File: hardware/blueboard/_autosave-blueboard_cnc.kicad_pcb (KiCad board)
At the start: 2 copper layers, 199.4 x 198.9 mm, 108 parts, among them Q1 TRANSISTOR_NPN, Q2 TRANSISTOR_NPN, Q3 TRANSISTOR_NPN, SW1 SW_SPST

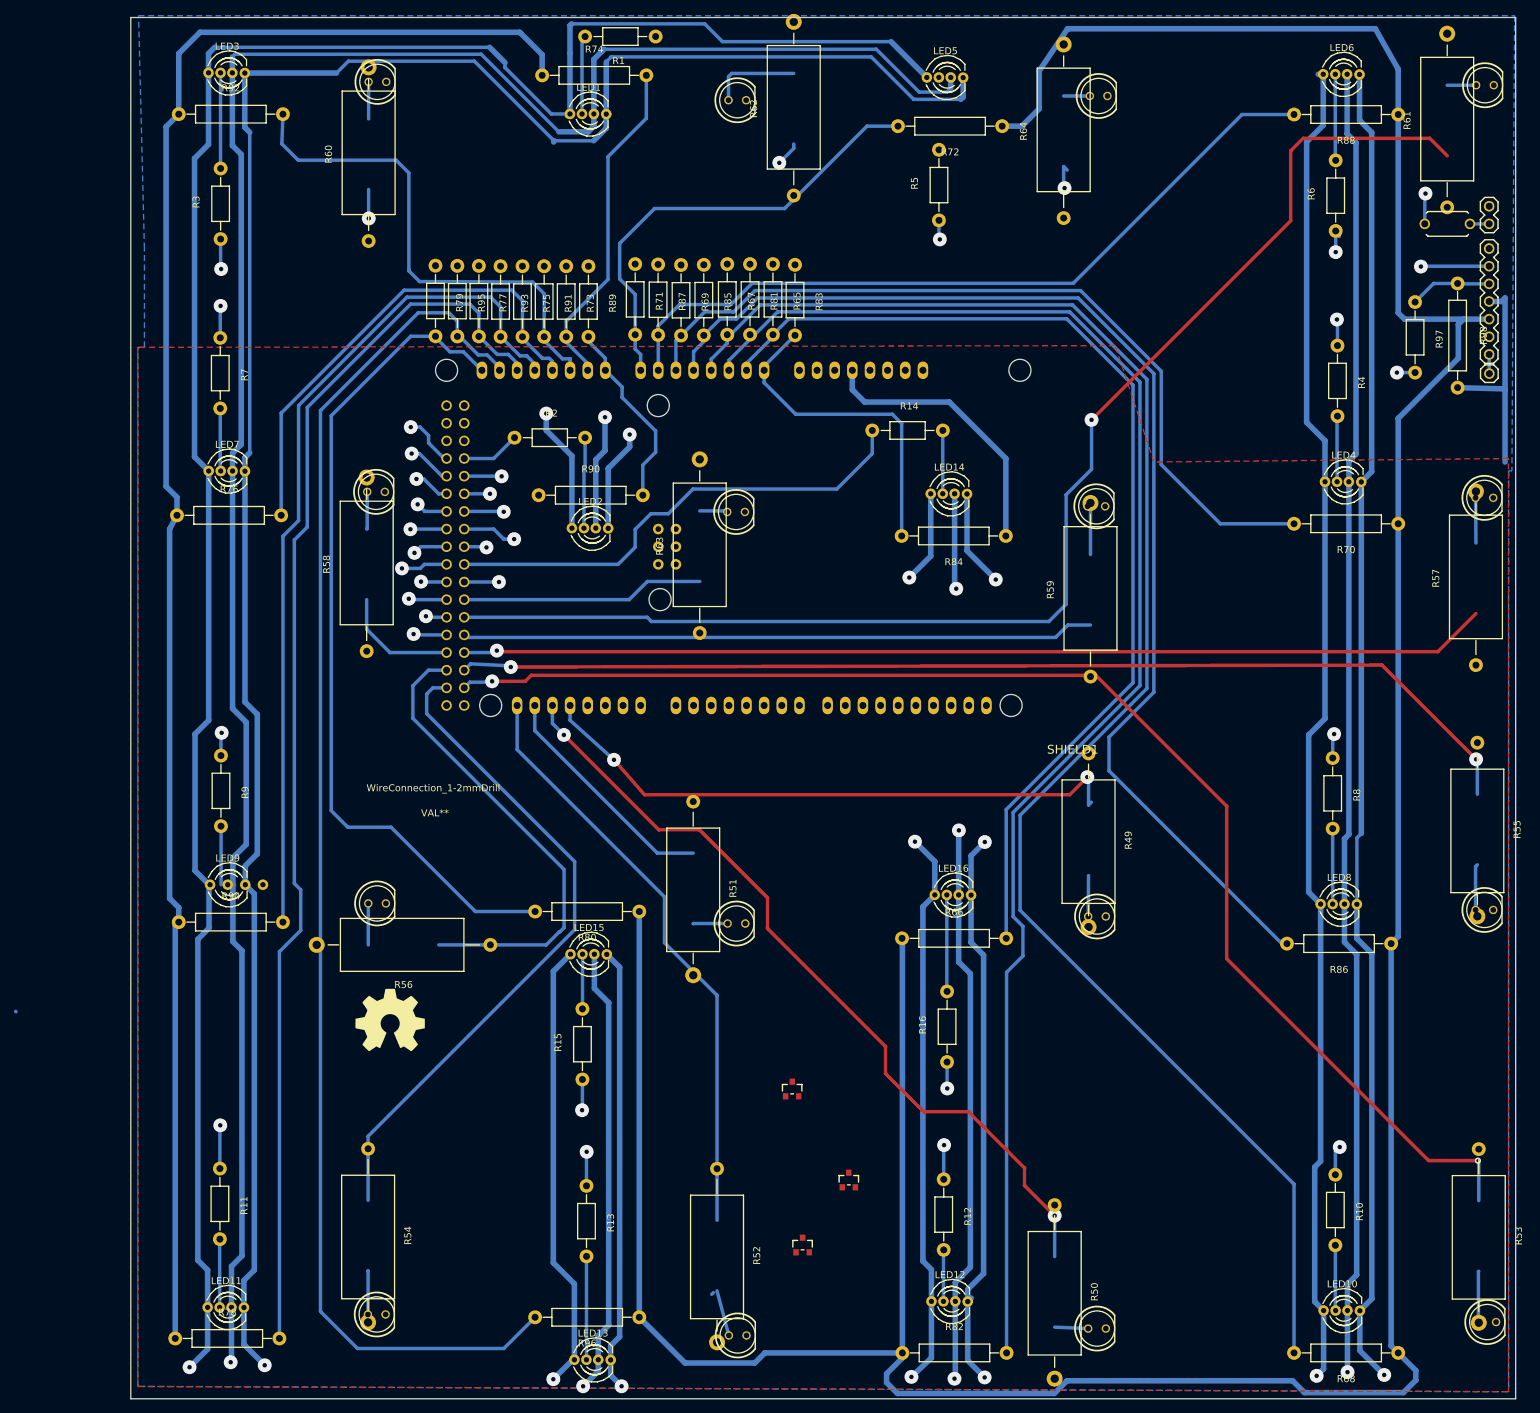
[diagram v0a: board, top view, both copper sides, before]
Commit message: state when board was cncd
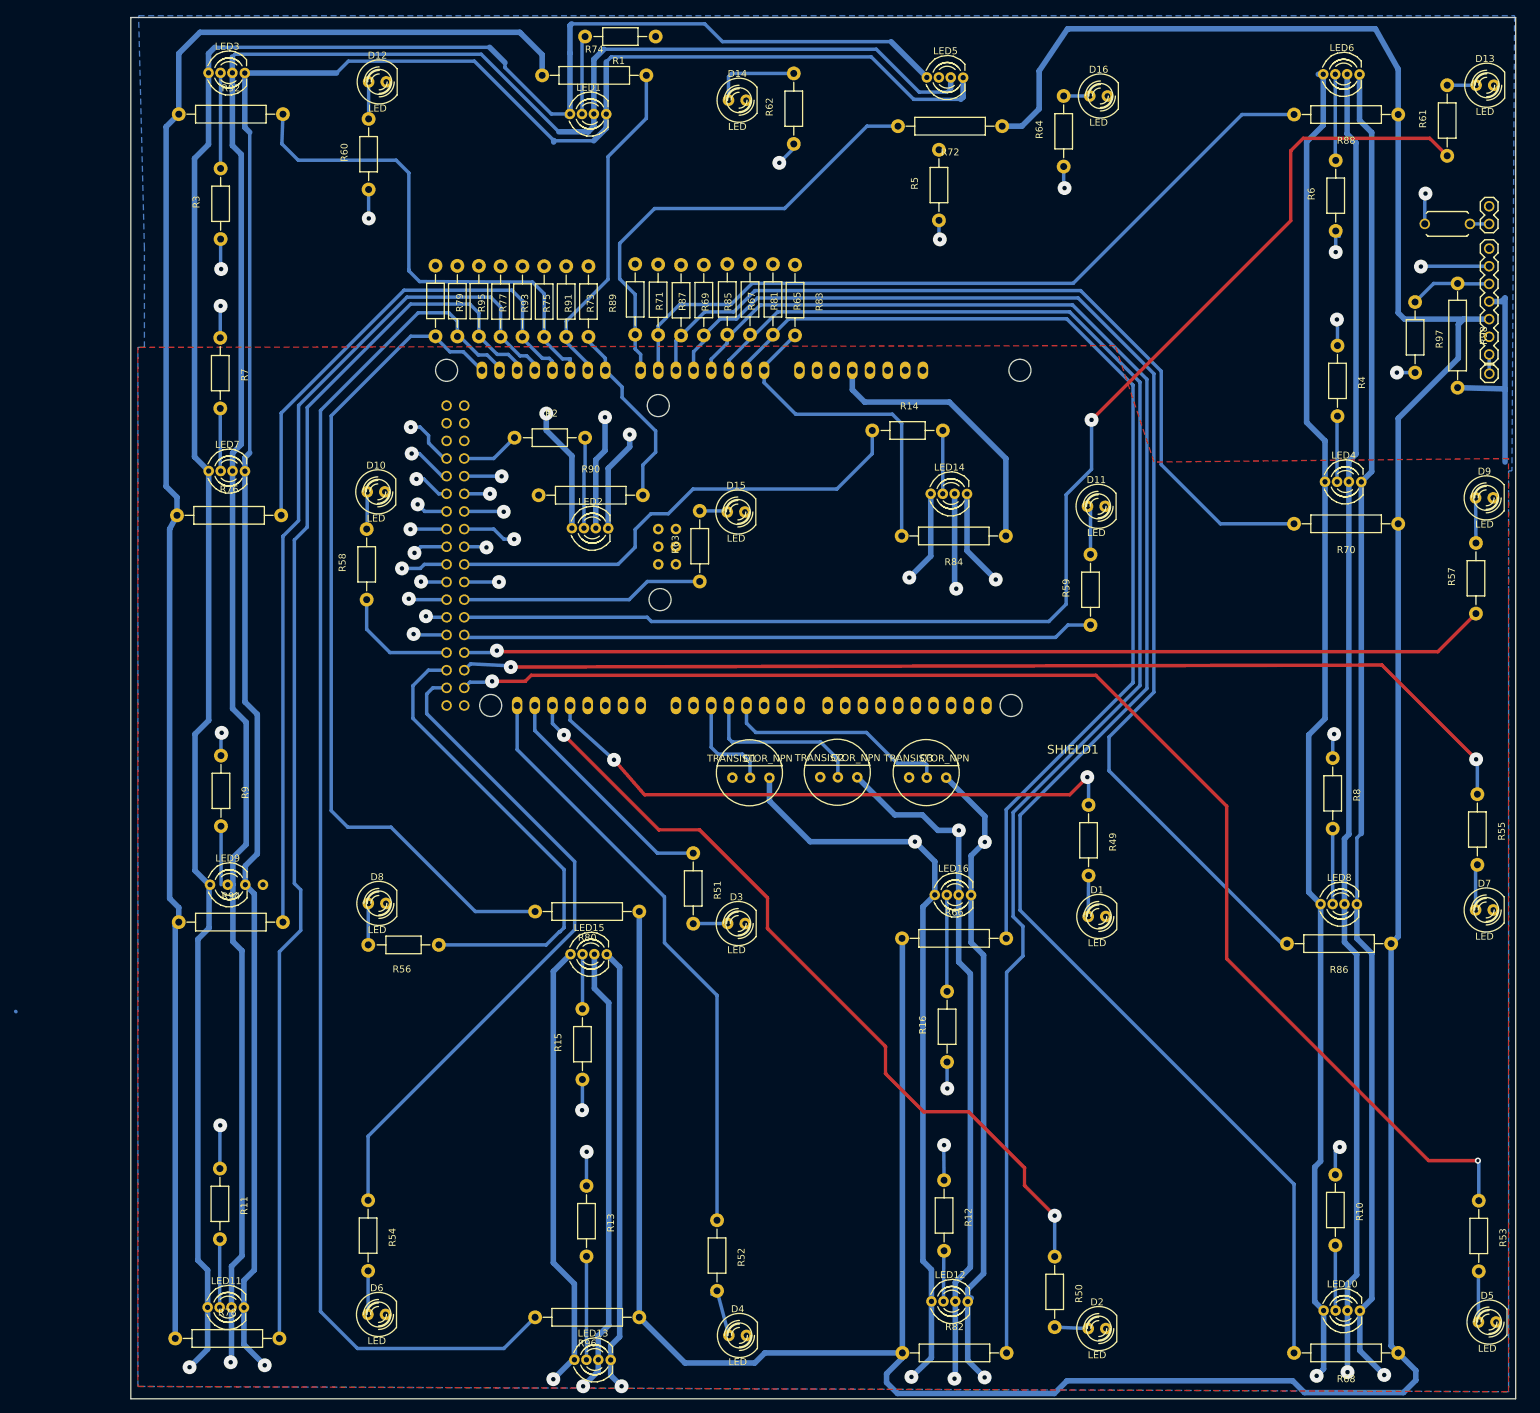
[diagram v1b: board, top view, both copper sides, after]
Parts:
- removed LOGO_OSHW_silkscreen_10mm: val**, Freetronics:LOGO_OSHW_silkscreen_10mm
- removed WireConnection_1-2mmDrill: VAL**, Wire_Connections_Bridges:WireConnection_1-2mmDrill
- D1, D10, D11, D12, D13, D14, D15, D16, D2, D3, D4, D5, D6, D7, D8, D9: footprint Freetronics:LED-5MM -> LEDs:LED-5MM
- Q1, Q2, Q3: footprint Freetronics:SOT23_TRANSISTOR -> finn_kicad:EBC-transistor-NPN
- R1, R10, R11, R12, R13, R14, R15, R16, R2, R3, R4, R5, R6, R7, R8, R9: value 470 -> 220
- R49, R50, R51, R52, R53, R54, R55, R56, R57, R58, R59, R60, R61, R62, R63, R64: footprint Resistors_ThroughHole:Resistor_Horizontal_RM25mm -> Resistors_ThroughHole:Resistor_Horizontal_RM10mm
- R65: value 4.7k -> R
- R67, R69, R71, R73, R75, R77, R79, R83, R85, R87, R89, R91, R93, R95: value 4.7 -> R
- moved Q1 70.5 mm to (186.7, 22.1)
- moved Q2 60.9 mm to (199.3, 22.0)
- moved Q3 51.5 mm to (212.1, 22.1)
- moved R12 0.14 mm to (214.6, 87.9)
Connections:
- R1 pad 2: Net-(LED1-PadA) -> Net-(LED16-PadA)
- R10 pad 2: Net-(LED10-PadA) -> Net-(LED9-PadA)
- R11 pad 2: Net-(LED11-PadA) -> Net-(LED10-PadA)
- R12 pad 2: Net-(LED12-PadA) -> Net-(LED11-PadA)
- R13 pad 1: Net-(R13-Pad1) -> Net-(LED15-PadA)
- R13 pad 2: Net-(LED13-PadA) -> Net-(R13-Pad2)
- R14 pad 1: Net-(R14-Pad1) -> Net-(LED14-PadA)
- R14 pad 2: Net-(LED14-PadA) -> Net-(R14-Pad2)
- R15 pad 1: Net-(R15-Pad1) -> Net-(LED13-PadA)
- R15 pad 2: Net-(LED15-PadA) -> Net-(R15-Pad2)
- R16 pad 1: Net-(R16-Pad1) -> Net-(LED12-PadA)
- R16 pad 2: Net-(LED16-PadA) -> Net-(R16-Pad2)
- R2 pad 2: Net-(LED2-PadA) -> Net-(LED1-PadA)
- R3 pad 2: Net-(LED3-PadA) -> Net-(LED2-PadA)
- R4 pad 2: Net-(LED4-PadA) -> Net-(LED3-PadA)
- R49 pad 2: Net-(D1-PadA) -> Net-(D1-Pad1)
- R5 pad 2: Net-(LED5-PadA) -> Net-(LED4-PadA)
- R50 pad 2: Net-(D2-PadA) -> Net-(D2-Pad1)
- R51 pad 2: Net-(D3-PadA) -> Net-(D3-Pad1)
- R52 pad 2: Net-(D4-PadA) -> Net-(D4-Pad1)
- R53 pad 2: Net-(D5-PadA) -> Net-(D5-Pad1)
- R54 pad 2: Net-(D6-PadA) -> Net-(D6-Pad1)
- R55 pad 2: Net-(D7-PadA) -> Net-(D7-Pad1)
- R56 pad 2: Net-(D8-PadA) -> Net-(D8-Pad1)
- R57 pad 2: Net-(D9-PadA) -> Net-(D9-Pad1)
- R58 pad 2: Net-(D10-PadA) -> Net-(D10-Pad1)
- R59 pad 2: Net-(D11-PadA) -> Net-(D11-Pad1)
- R6 pad 2: Net-(LED6-PadA) -> Net-(LED5-PadA)
- R60 pad 2: Net-(D12-PadA) -> Net-(D12-Pad1)
- R61 pad 2: Net-(D13-PadA) -> Net-(D13-Pad1)
- R62 pad 2: Net-(D14-PadA) -> Net-(D14-Pad1)
- R63 pad 2: Net-(D15-PadA) -> Net-(D15-Pad1)
- R64 pad 2: Net-(D16-PadA) -> Net-(D16-Pad1)
- R7 pad 2: Net-(LED7-PadA) -> Net-(LED6-PadA)
- R8 pad 2: Net-(LED8-PadA) -> Net-(LED7-PadA)
- R9 pad 2: Net-(LED9-PadA) -> Net-(LED8-PadA)
- SHIELD1 pad 2: Net-(Q3-PadB) -> Net-(Q1-PadB)
- SHIELD1 pad 34: Net-(R16-Pad1) -> Net-(R13-Pad2)
- SHIELD1 pad 35: Net-(R15-Pad1) -> Net-(R14-Pad2)
- SHIELD1 pad 36: Net-(R14-Pad1) -> Net-(R15-Pad2)
- SHIELD1 pad 37: Net-(R13-Pad1) -> Net-(R16-Pad2)
- SHIELD1 pad 4: Net-(Q1-PadB) -> Net-(Q3-PadB)
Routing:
- net Net-(R59-Pad1): track 275.0 -> 91.1 mm, vias 1 -> 0
- net Net-(R53-Pad1): track 10.4 -> 194.3 mm, vias 1 -> 2
- net Net-(R14-Pad1): track 70.2 -> 0.00 mm
- net Net-(LED14-PadA): track 9.12 -> 57.1 mm
- net Net-(Q3-PadB): track 0.00 -> 32.9 mm
- net Net-(R15-Pad2): track 0.00 -> 30.0 mm
- net R: track 689.6 -> 716.4 mm
- net Net-(Q2-PadB): track 0.00 -> 24.3 mm
- net G: track 682.6 -> 700.4 mm
- net Net-(Q1-PadB): track 0.00 -> 14.8 mm
- net Net-(D14-PadA): track 13.2 -> 0.00 mm
- net Net-(D14-Pad1): track 0.00 -> 13.2 mm
- net (no net): track 12.1 -> 0.07 mm, vias 3 -> 0
- net Net-(R13-Pad1): track 11.6 -> 0.00 mm, vias 2 -> 0
- net B: track 596.4 -> 608.0 mm
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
